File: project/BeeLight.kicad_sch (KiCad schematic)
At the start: 23 parts, among them IC101 BT40F, IC102 APDS-9306-065, IC103 BME688, Q101 BSS84, SW101 JOIN, X102 DEBUG

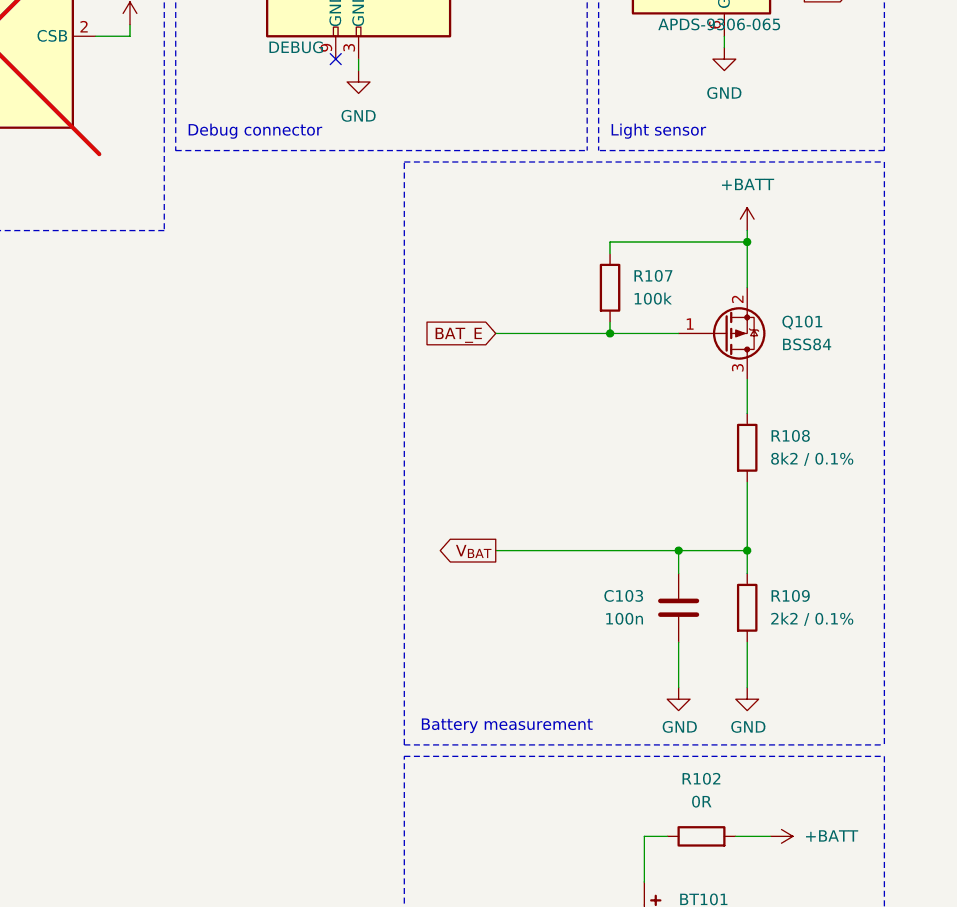
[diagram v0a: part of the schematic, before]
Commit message: Firmware is compiling with custom board, testing first hardware release
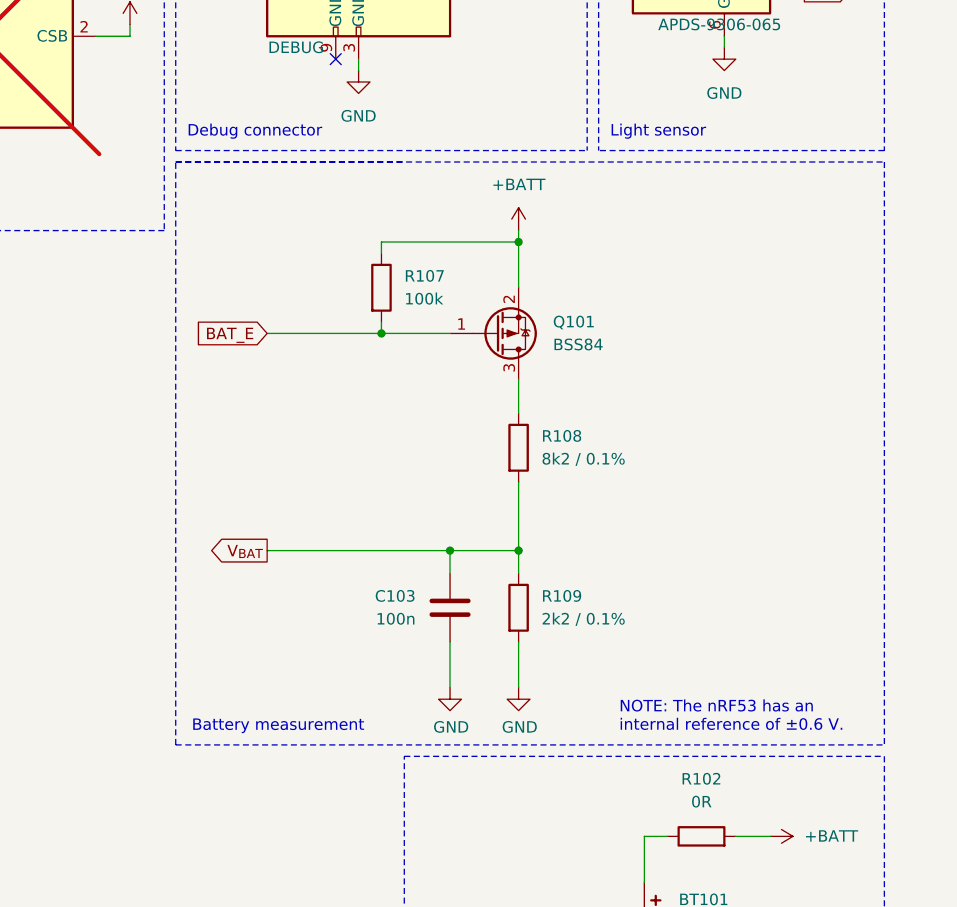
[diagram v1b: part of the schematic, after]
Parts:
- Q101: footprint Package_TO_SOT_SMD:SOT-23 -> Package_TO_SOT_SMD:SOT-23-3
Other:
- note added: "NOTE: The nRF53 has an internal reference of ±0.6 V."
- moved on the sheet: C103, Q101, R107, R108, R109

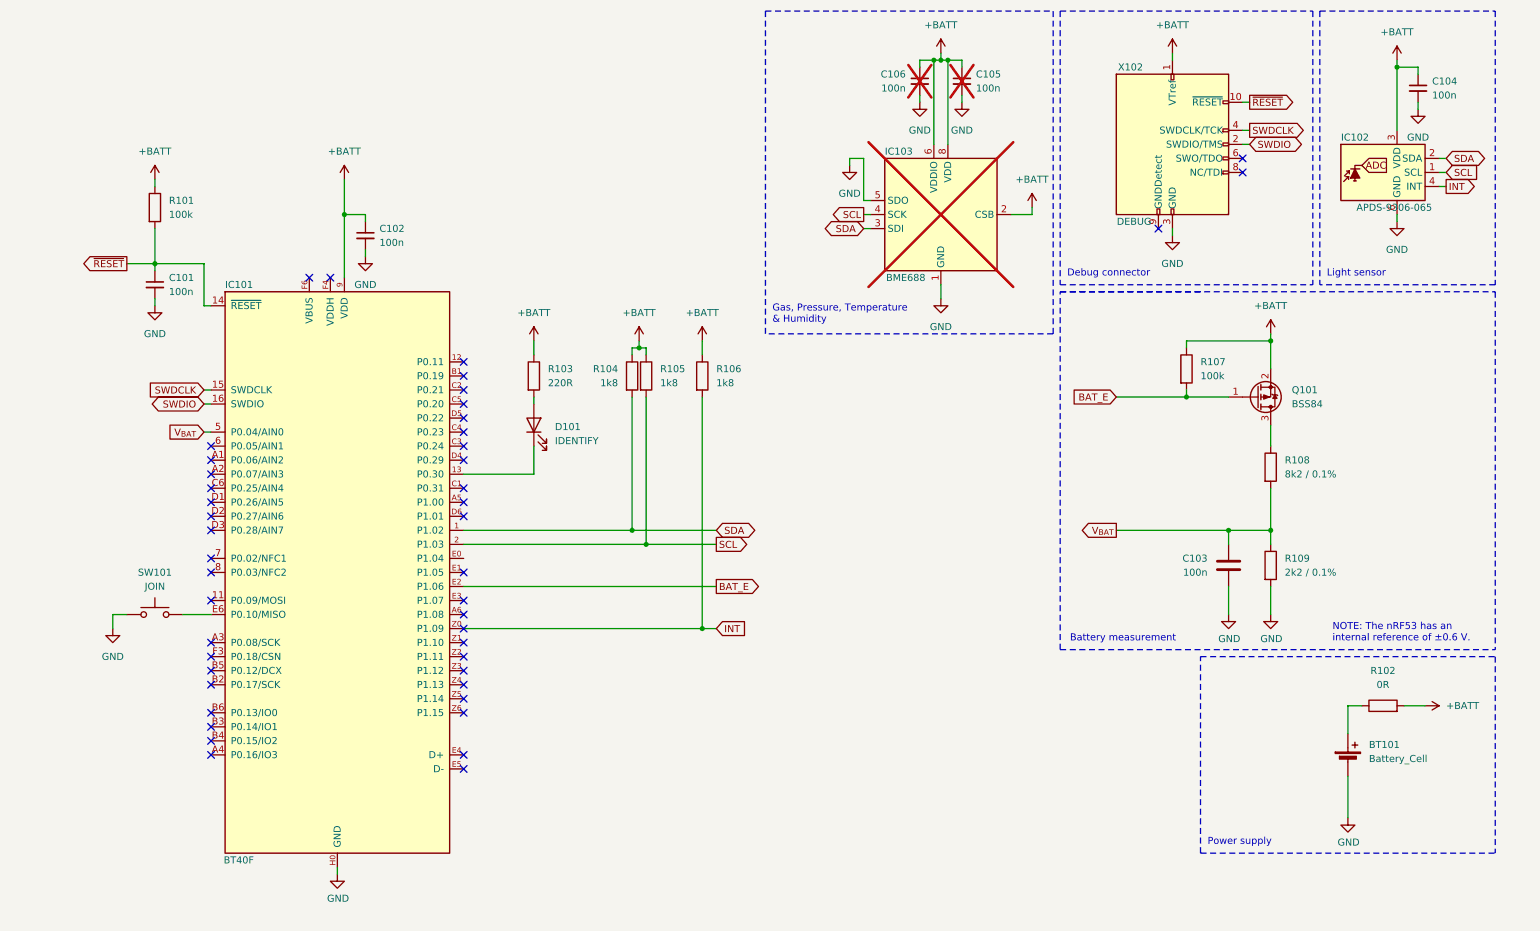
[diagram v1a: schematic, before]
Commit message: - Replace nRF53 with nRF54L - Working on version 2 with BME688
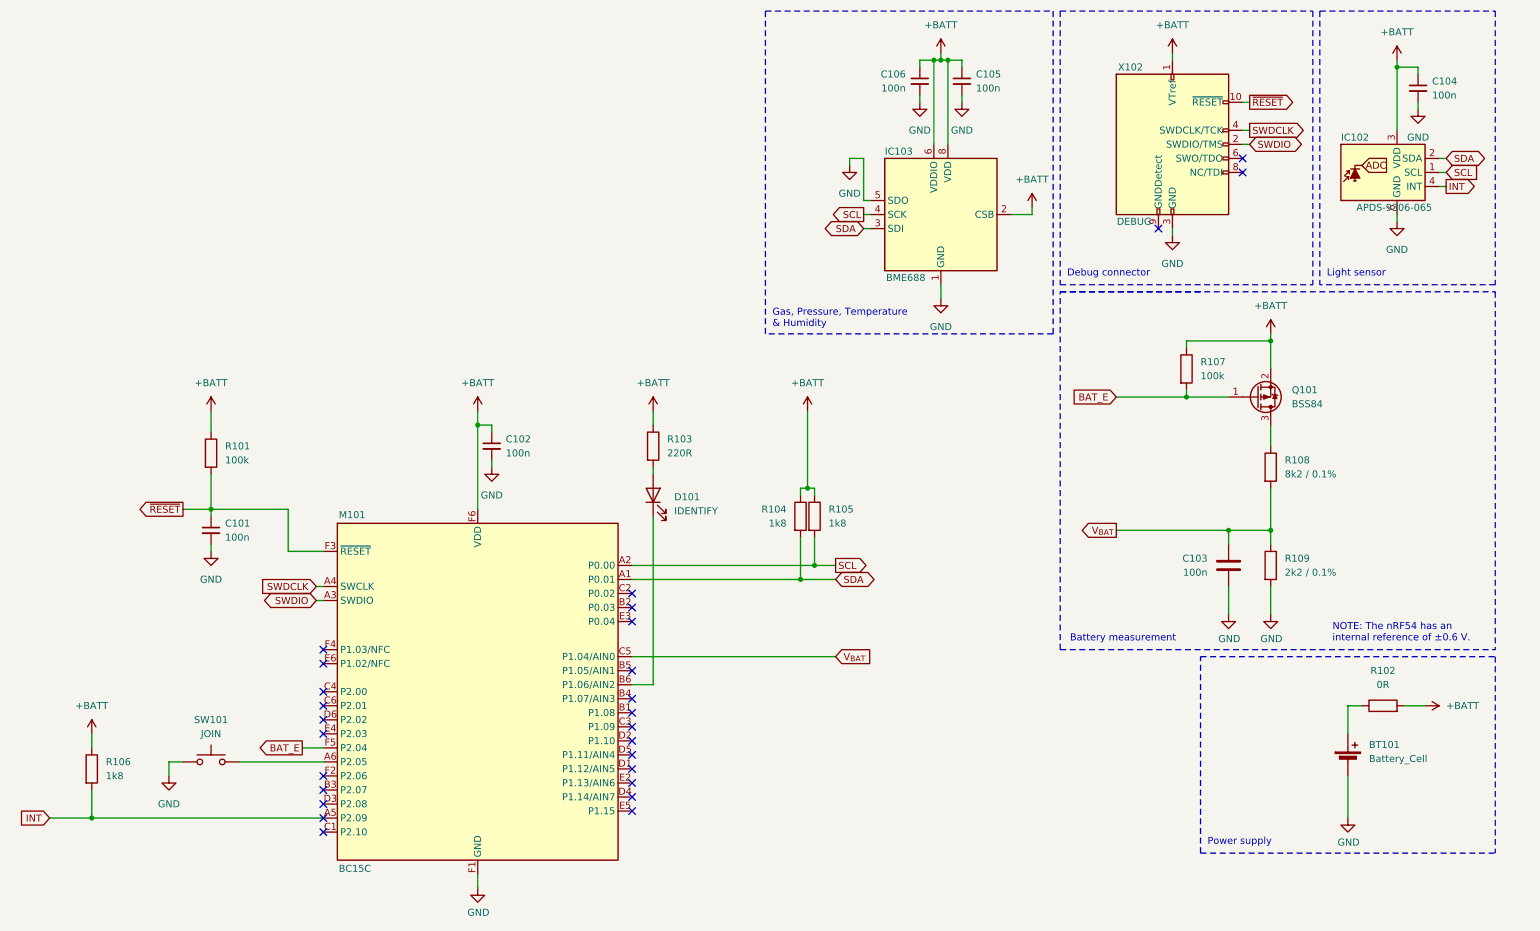
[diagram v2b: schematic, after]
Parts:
- removed IC101: BT40F, Fanstel:XCVR_BT40F, symbol Fanstel:BT40F
- added M101: BC15C, Fanstel:BC15C, symbol Fanstel:BC15C
- C105, C106, IC103: now fitted; now in the parts list
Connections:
- net +BATT: now also M101.F6 (VDD)
- net BAT_E: now also M101.F5 (P2.04)
- net GND: now also M101.E1 (GND), M101.F1 (GND)
- net INT: now also M101.A5 (P2.09)
- net SCL: now also M101.A2 (P0.00)
- net SDA: now also M101.A1 (P0.01)
- net SWDCLK: now also M101.A4 (SWCLK)
- net SWDIO: now also M101.A3 (SWDIO)
- net V_{BAT}: now also M101.C5 (P1.04/AIN0)
- net ~{RESET}: now also M101.F3 (~{RESET})
- net at D101.1 (K): now also M101.B6 (P1.06/AIN2)
- net at SW101.2: now also M101.A6 (P2.05)
- no-connect marks 46 -> 27
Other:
- note added: "NOTE: The nRF54 has an internal reference of ±0.6 V."
- note removed: "NOTE: The nRF53 has an internal reference of ±0.6 V."
- title: BeeLight -> BeeLight v2
- moved on the sheet: C101, C102, D101, R101, R103, R104, R105, R106, SW101

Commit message: Switch to BM15C module
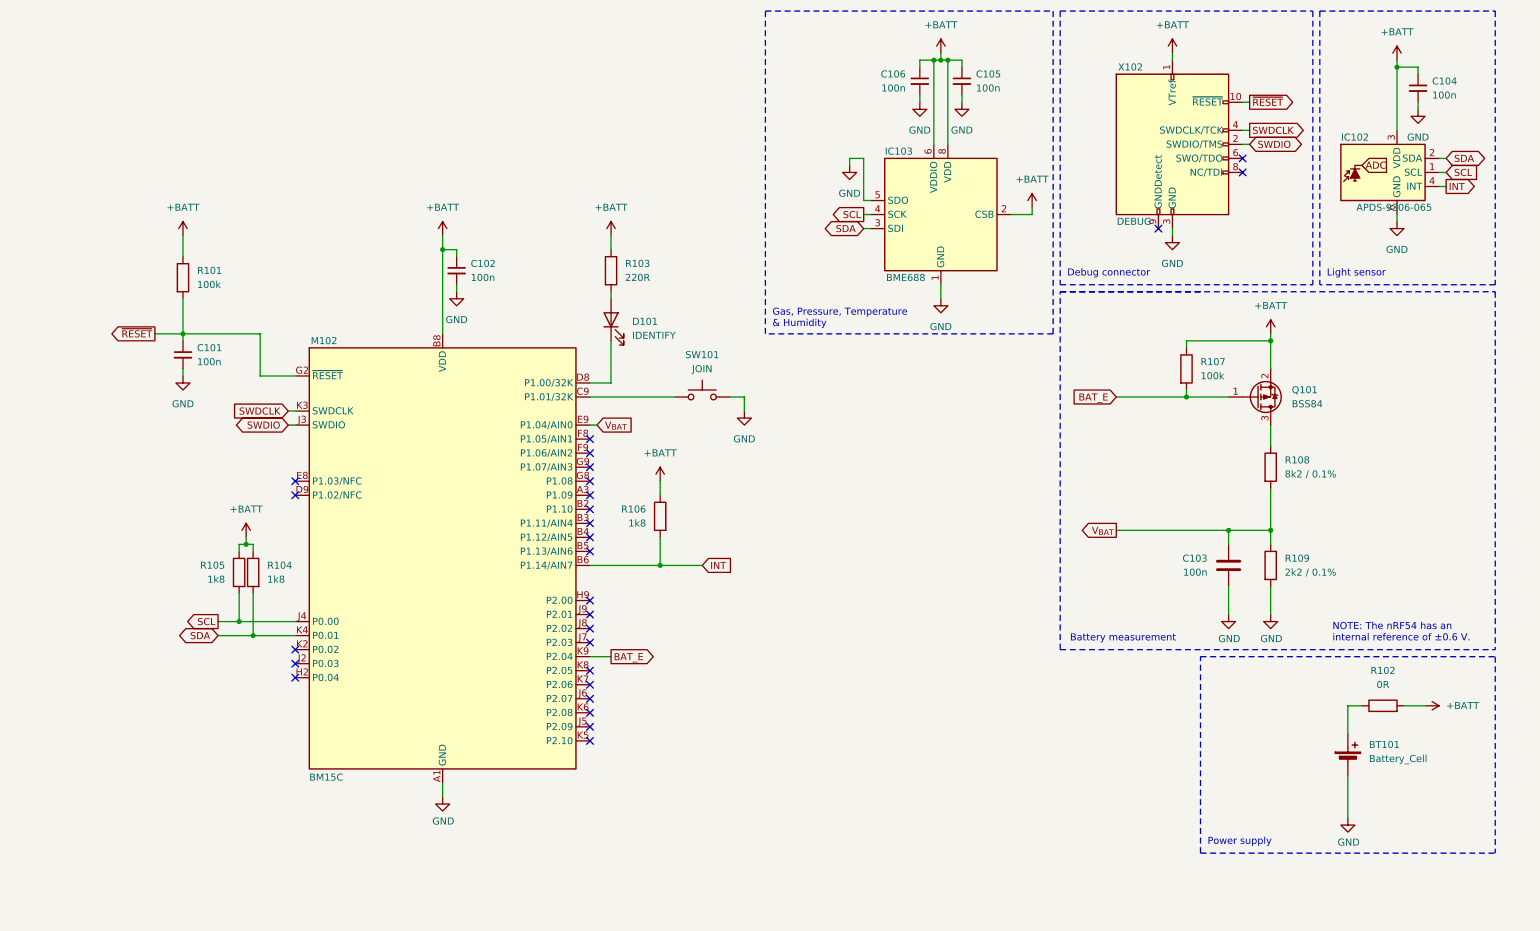
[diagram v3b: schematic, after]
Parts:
- removed M101: BC15C, Fanstel:BC15C, symbol Fanstel:BC15C
- added M102: BM15C, Fanstel:BM15C, symbol Fanstel:BM15C
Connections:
- net +BATT: now also M102.B8 (VDD), M102.C8 (VDD)
- net BAT_E: now also M102.K9 (P2.04)
- net GND: now also M102.A1 (GND), M102.A9 (GND), M102.B1 (GND), M102.B7 (GND), M102.B9 (GND), M102.D1 (GND), M102.E1 (GND), M102.F1 (GND), M102.H8 (GND)
- net INT: now also M102.B6 (P1.14/AIN7)
- net SCL: now also M102.J4 (P0.00)
- net SDA: now also M102.K4 (P0.01)
- net SWDCLK: now also M102.K3 (SWDCLK)
- net SWDIO: now also M102.J3 (SWDIO)
- net V_{BAT}: now also M102.E9 (P1.04/AIN0)
- net ~{RESET}: now also M102.G2 (~{RESET})
- net at D101.1 (K): now also M102.D8 (P1.00/32K)
- net at SW101.2: now also M102.C9 (P1.01/32K)
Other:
- moved on the sheet: C101, C102, D101, R101, R103, R104, R105, R106, SW101

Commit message: Replace nRF54 module
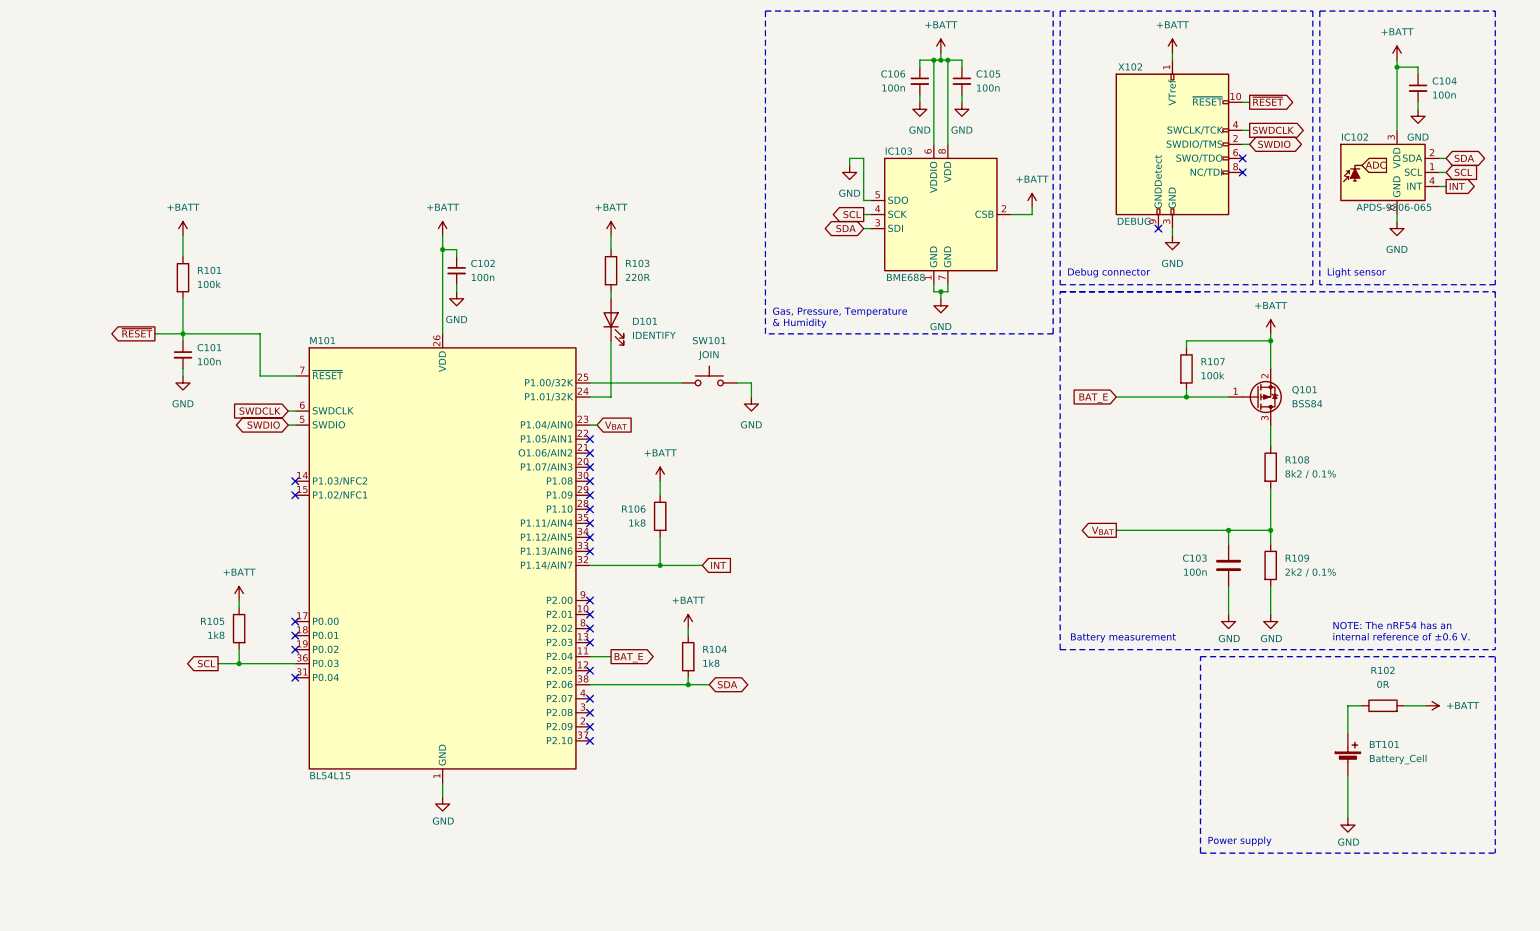
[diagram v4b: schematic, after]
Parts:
- removed M102: BM15C, Fanstel:BM15C, symbol Fanstel:BM15C
- added M101: BL54L15, Ezurio:BL54L15, symbol Ezurio:BL54L15
- IC103: footprint Bosch:Bosch_LGA-8_3x3mm_P0.8mm_ClockwisePinNumbering -> Package_LGA_Kampi:Bosch_LGA-8_3x3mm_P0.8mm_ClockwisePinNumbering
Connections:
- net +BATT: now also M101.26 (VDD)
- net BAT_E: now also M101.11 (P2.04)
- net GND: now also M101.1 (GND), M101.16 (GND), M101.27 (GND), M101.39 (GND)
- net INT: now also M101.32 (P1.14/AIN7)
- net SCL: now also M101.36 (P0.03)
- net SDA: now also M101.38 (P2.06)
- net SWDCLK: now also M101.6 (SWDCLK)
- net SWDIO: now also M101.5 (SWDIO)
- net V_{BAT}: now also M101.23 (P1.04/AIN0)
- net ~{RESET}: now also M101.7 (~{RESET})
- net at D101.1 (K): now also M101.24 (P1.01/32K)
- net at SW101.2: now also M101.25 (P1.00/32K)
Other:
- moved on the sheet: R104, R105, SW101
